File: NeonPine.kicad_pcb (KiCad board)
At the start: 2 copper layers, 54.7 x 69 mm, 74 parts, among them J1 USB-C 6P (USB4125-GF-A), J2 SWD pogo pads, Q1 DMN15H310SE, Q11 MMBTA42, Q12 MMBTA42, Q13 MMBTA42, Q14 MMBTA42, Q15 MMBTA42, Q16 MMBTA42, Q17 MMBTA42, Q18 MMBTA42, Q19 MMBTA42, Q2 TEPT4400, Q20 MMBTA42, U1 CH32V003F4P6

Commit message: incomplete big package ver
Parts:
- added C10: 100n, Capacitor_SMD:C_0603_1608Metric, B.Cu at (111.8, 84.1)
- added C9: 100n, Capacitor_SMD:C_0603_1608Metric, B.Cu at (96.1, 84.1)
- added Q21: MMBTA42, Package_TO_SOT_SMD:SOT-23, B.Cu at (101.6, 54.0)
- added Q22: MMBTA42, Package_TO_SOT_SMD:SOT-23, B.Cu at (97.1, 67.5)
- added Q23: MMBTA42, Package_TO_SOT_SMD:SOT-23, B.Cu at (106.1, 67.5)
- added Q24: MMBTA42, Package_TO_SOT_SMD:SOT-23, B.Cu at (93.6, 80.0)
- added Q25: MMBTA42, Package_TO_SOT_SMD:SOT-23, B.Cu at (101.6, 80.0)
- added Q26: MMBTA42, Package_TO_SOT_SMD:SOT-23, B.Cu at (109.6, 80.0)
- added Q27: MMBTA42, Package_TO_SOT_SMD:SOT-23, B.Cu at (87.6, 92.3)
- added Q28: MMBTA42, Package_TO_SOT_SMD:SOT-23, B.Cu at (96.6, 92.3)
- added Q29: MMBTA42, Package_TO_SOT_SMD:SOT-23, B.Cu at (106.6, 92.3)
- added Q30: MMBTA42, Package_TO_SOT_SMD:SOT-23, B.Cu at (115.6, 92.3)
- added R31: 150k, Resistor_SMD:R_0805_2012Metric, B.Cu at (98.4, 50.7)
- added R32: 150k, Resistor_SMD:R_0805_2012Metric, B.Cu at (93.9, 64.2)
- added R33: 150k, Resistor_SMD:R_0805_2012Metric, B.Cu at (102.9, 64.2)
- added R34: 150k, Resistor_SMD:R_0805_2012Metric, B.Cu at (90.4, 76.7)
- added R35: 150k, Resistor_SMD:R_0805_2012Metric, B.Cu at (98.4, 76.7)
- added R36: 150k, Resistor_SMD:R_0805_2012Metric, B.Cu at (106.4, 76.7)
- added R37: 150k, Resistor_SMD:R_0805_2012Metric, B.Cu at (84.4, 89.0)
- added R38: 150k, Resistor_SMD:R_0805_2012Metric, B.Cu at (93.4, 89.0)
- added R39: 150k, Resistor_SMD:R_0805_2012Metric, B.Cu at (103.4, 89.0)
- added R40: 150k, Resistor_SMD:R_0805_2012Metric, B.Cu at (112.4, 89.0)
- added R51: 22k, Resistor_SMD:R_0402_1005Metric, B.Cu at (101.6, 56.8)
- added R52: 22k, Resistor_SMD:R_0402_1005Metric, B.Cu at (97.1, 70.2)
- added R53: 22k, Resistor_SMD:R_0402_1005Metric, B.Cu at (106.1, 70.2)
- added R54: 22k, Resistor_SMD:R_0402_1005Metric, B.Cu at (93.6, 82.8)
- added R55: 22k, Resistor_SMD:R_0402_1005Metric, B.Cu at (101.6, 82.8)
- added R56: 22k, Resistor_SMD:R_0402_1005Metric, B.Cu at (109.6, 82.8)
- added R57: 22k, Resistor_SMD:R_0402_1005Metric, B.Cu at (87.6, 95.0)
- added R58: 22k, Resistor_SMD:R_0402_1005Metric, B.Cu at (96.6, 95.0)
- added R59: 22k, Resistor_SMD:R_0402_1005Metric, B.Cu at (106.6, 95.0)
- added R60: 22k, Resistor_SMD:R_0402_1005Metric, B.Cu at (115.6, 95.0)
- added U2: 74HC595BQ, Package_DFN_QFN:DHVQFN-16-1EP_2.5x3.5mm_P0.5mm_EP1x2mm, B.Cu at (99.8, 86.2)
- added U3: 74HC595BQ, Package_DFN_QFN:DHVQFN-16-1EP_2.5x3.5mm_P0.5mm_EP1x2mm, B.Cu at (119.4, 91.8)
- D1: value ES1D -> 200V 1A fast SOD-123F (verify P/N); footprint Diode_SMD:D_SMA -> Diode_SMD:D_SOD-123F
- D2: value SMAJ100A -> SMF100A; footprint Diode_SMD:D_SMA -> Diode_SMD:D_SOD-123F
- R41, R42, R43, R44, R45, R46, R47, R48, R49, R50: footprint Resistor_SMD:R_0603_1608Metric -> Resistor_SMD:R_0402_1005Metric
- TP3: value BUZZ/spare -> SR_CLK test
- moved D2 31.4 mm to (90.0, 107.2)
- moved TP3 30.8 mm to (90.8, 86.8), turned to -90 degrees
- moved C2 23.6 mm to (122.9, 92.9), turned to 0 degrees
- moved C1 22.4 mm to (122.9, 94.7)
- moved C4 21.2 mm to (93.0, 107.2), turned to -90 degrees
- moved J2 17.0 mm to (109.5, 91.8), turned to -90 degrees
- moved R7 14.9 mm to (104.3, 76.3)
- moved R4 14.4 mm to (108.6, 107.4)
- moved FB1 13.6 mm to (115.1, 84.1)
- moved R11 12.0 mm to (92.1, 96.1), turned to 90 degrees
- moved R3 8.93 mm to (100.0, 89.7), turned to 180 degrees
- moved R12 8.85 mm to (99.8, 96.4), turned to 0 degrees
- moved R5 7.24 mm to (103.8, 84.1), turned to 0 degrees
- moved R2 7.15 mm to (105.0, 107.4), turned to 0 degrees
- moved R9 6.65 mm to (90.3, 96.0), turned to 90 degrees
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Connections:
- net /B1 renamed Net-(Q11-B)
- net /B10 renamed Net-(Q20-B)
- net /B2 renamed Net-(Q12-B)
- net /B3 renamed Net-(Q13-B)
- net /B4 renamed Net-(Q14-B)
- net /B5 renamed Net-(Q15-B)
- net /B6 renamed Net-(Q16-B)
- net /B7 renamed Net-(Q17-B)
- net /B8 renamed Net-(Q18-B)
- net /B9 renamed Net-(Q19-B)
- net /BUZZ renamed /SR_CLK
- U1 pad 1: /LAMP10 -> /SR_LATCH
- U1 pad 12: /LAMP2 -> /LAMP5
- U1 pad 13: /LAMP5 -> /LAMP9
- U1 pad 14: /LAMP1 -> /LAMP2
- U1 pad 15: /LAMP9 -> /LAMP3
- U1 pad 16: /LAMP3 -> /LAMP6
- U1 pad 17: /LAMP6 -> /LAMP10
- U1 pad 3: unconnected-(U1-PD6-Pad3) -> /SR_DATA
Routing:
- net GND: track 208.0 -> 297.2 mm, vias 7 -> 11
- net /HV+: track 114.3 -> 176.8 mm, vias 0 -> 9
- net /SR_CLK: track 23.6 -> 68.0 mm
- net /SR_CHAIN: track 0.00 -> 31.9 mm, vias 0 -> 3
- net /LAMPA1: track 0.00 -> 30.1 mm, vias 0 -> 2
- net /VBUS_F: track 45.7 -> 16.8 mm, vias 6 -> 3
- net +5V: track 101.6 -> 129.1 mm, vias 5 -> 6
- net /LAMPA7: track 0.00 -> 24.0 mm, vias 0 -> 3
- net /LAMP1: track 58.4 -> 37.1 mm
- net /SWIO: track 31.2 -> 11.4 mm
- net /CC2: track 25.4 -> 5.78 mm
- net /LAMPA3: track 0.00 -> 19.2 mm, vias 0 -> 3
- net /CC1: track 45.8 -> 27.3 mm, vias 4 -> 3
- net /VFB: track 15.5 -> 33.8 mm, vias 2 -> 4
- net /LAMPA6: track 0.00 -> 16.7 mm, vias 0 -> 2
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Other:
- copper layers 2 -> 4

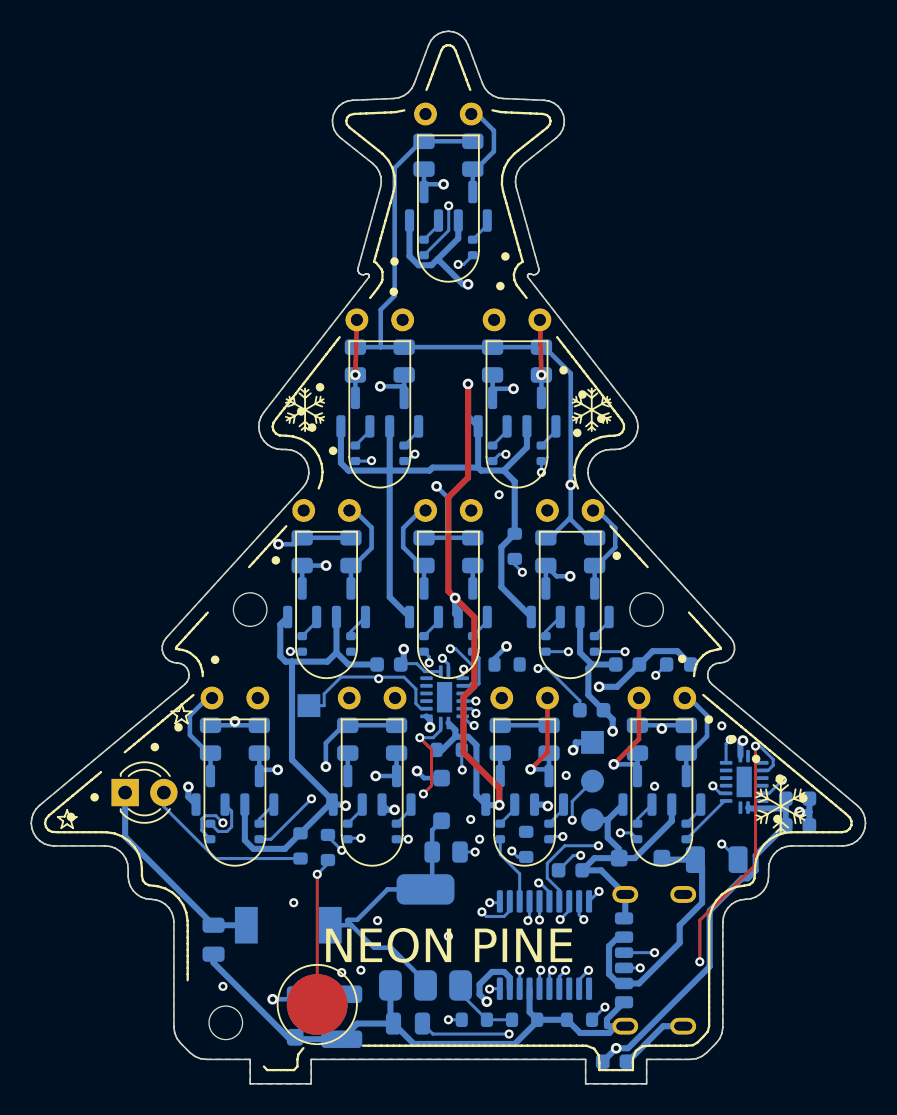
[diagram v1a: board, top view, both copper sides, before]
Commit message: 2Layer routing complete
needs cleanup
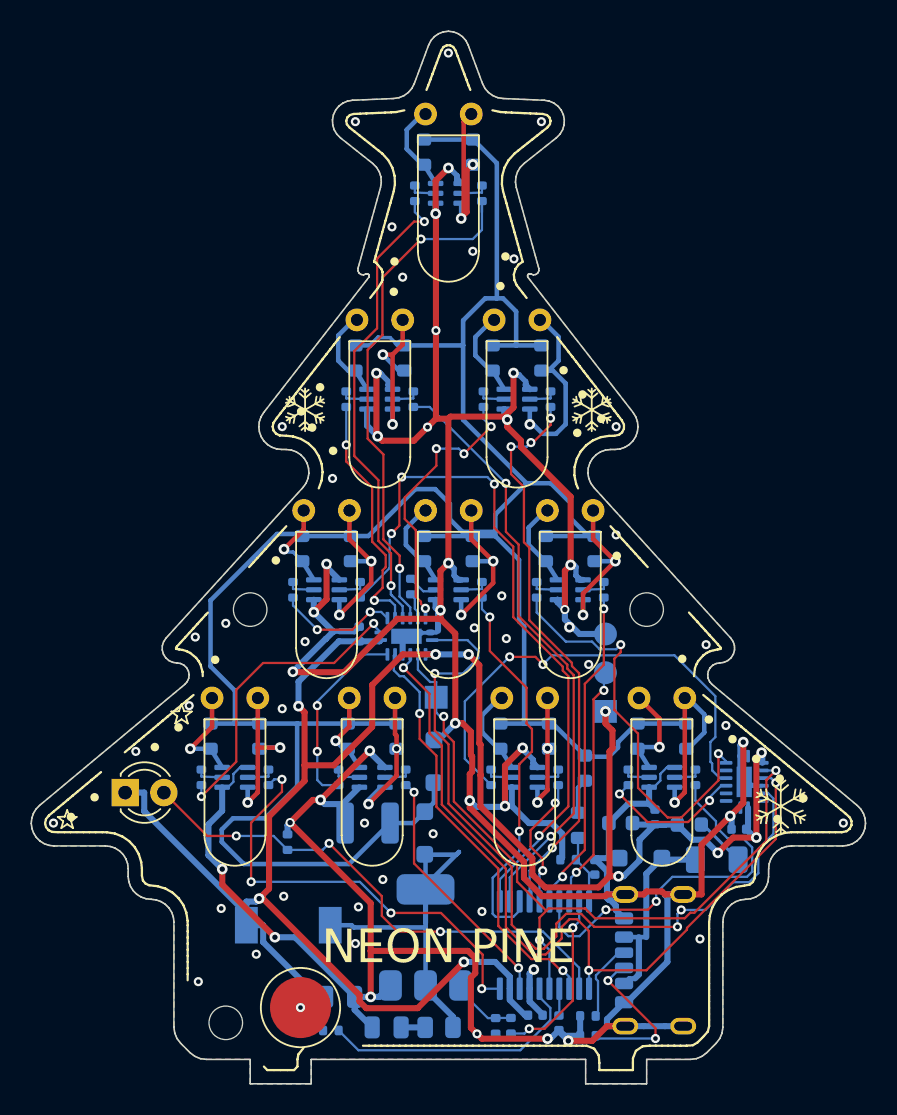
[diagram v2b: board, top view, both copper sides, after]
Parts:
- removed Q21, Q22, Q23, Q24, Q25, Q26, Q27, Q28, Q29, Q30: MMBTA42, Package_TO_SOT_SMD:SOT-23
- C10, C2, C5, C6, C7, C9: footprint Capacitor_SMD:C_0603_1608Metric -> Capacitor_SMD:C_0402_1005Metric
- Q11, Q12, Q13, Q14, Q15, Q16, Q17, Q18, Q19, Q20: value MMBTA42 -> MMDT5551; footprint Package_TO_SOT_SMD:SOT-23 -> Package_TO_SOT_SMD:SOT-363_SC-70-6
- R1, R11, R2, R3, R4, R7, R9: footprint Resistor_SMD:R_0603_1608Metric -> Resistor_SMD:R_0402_1005Metric
- R21, R22, R23, R24, R25, R26, R27, R28, R29, R30, R31, R32, R33, R34, R35, R36, R37, R38, R39, R40: value 150k -> 150k 200V; footprint Resistor_SMD:R_0805_2012Metric -> Resistor_SMD:R_0603_1608Metric
- U2, U3: footprint Package_DFN_QFN:DHVQFN-16-1EP_2.5x3.5mm_P0.5mm_EP1x2mm -> NeonPine:DHVQFN-16-1EP_2.5x3.5mm_P0.5mm_EP1x2mm_EPGND
- moved R7 20.8 mm to (107.8, 96.9), turned to 180 degrees
- moved R3 19.7 mm to (109.2, 107.2)
- moved D2 19.0 mm to (99.0, 90.5), turned to 90 degrees
- moved C10 13.0 mm to (119.0, 94.9)
- moved C4 12.8 mm to (94.7, 94.5), turned to 180 degrees
- moved R11 12.0 mm to (92.3, 108.1), turned to 0 degrees
- moved C1 11.6 mm to (111.3, 94.5), turned to 180 degrees
- moved R12 11.5 mm to (99.4, 107.9), turned to 180 degrees
- moved FB1 10.5 mm to (115.8, 94.6), turned to 180 degrees
- moved C5 10.3 mm to (109.6, 97.4), turned to 90 degrees
- moved C7 10.0 mm to (107.2, 107.6), turned to -90 degrees
- moved C2 9.43 mm to (113.5, 94.1), turned to 90 degrees
- moved C3 9.11 mm to (92.9, 105.9), turned to 0 degrees
- moved R5 8.50 mm to (109.0, 90.9), turned to -90 degrees
- moved TP3 8.37 mm to (99.2, 86.2), turned to 180 degrees
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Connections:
- LA1 pad 1: Net-(Q11-C) -> Net-(Q11A-C1)
- LA1 pad 2: Net-(Q21-C) -> Net-(Q11B-C2)
- LA10 pad 1: Net-(Q20-C) -> Net-(Q20A-C1)
- LA10 pad 2: Net-(Q30-C) -> Net-(Q20B-C2)
- LA2 pad 1: Net-(Q12-C) -> Net-(Q12A-C1)
- LA2 pad 2: Net-(Q22-C) -> Net-(Q12B-C2)
- LA3 pad 1: Net-(Q13-C) -> Net-(Q13A-C1)
- LA3 pad 2: Net-(Q23-C) -> Net-(Q13B-C2)
- LA4 pad 1: Net-(Q14-C) -> Net-(Q14A-C1)
- LA4 pad 2: Net-(Q24-C) -> Net-(Q14B-C2)
- LA5 pad 1: Net-(Q15-C) -> Net-(Q15A-C1)
- LA5 pad 2: Net-(Q25-C) -> Net-(Q15B-C2)
- LA6 pad 1: Net-(Q16-C) -> Net-(Q16A-C1)
- LA6 pad 2: Net-(Q26-C) -> Net-(Q16B-C2)
- LA7 pad 1: Net-(Q17-C) -> Net-(Q17A-C1)
- LA7 pad 2: Net-(Q27-C) -> Net-(Q17B-C2)
- LA8 pad 1: Net-(Q18-C) -> Net-(Q18A-C1)
- LA8 pad 2: Net-(Q28-C) -> Net-(Q18B-C2)
- LA9 pad 1: Net-(Q19-C) -> Net-(Q19A-C1)
- LA9 pad 2: Net-(Q29-C) -> Net-(Q19B-C2)
- Q11 pad 1: Net-(Q11-B) -> GND
- Q11 pad 2: GND -> Net-(Q11A-B1)
- Q11 pad 3: Net-(Q11-C) -> Net-(Q11B-C2)
- Q12 pad 1: Net-(Q12-B) -> GND
- Q12 pad 2: GND -> Net-(Q12A-B1)
- Q12 pad 3: Net-(Q12-C) -> Net-(Q12B-C2)
- Q13 pad 1: Net-(Q13-B) -> GND
- Q13 pad 2: GND -> Net-(Q13A-B1)
- Q13 pad 3: Net-(Q13-C) -> Net-(Q13B-C2)
- Q14 pad 1: Net-(Q14-B) -> GND
- Q14 pad 2: GND -> Net-(Q14A-B1)
- Q14 pad 3: Net-(Q14-C) -> Net-(Q14B-C2)
- Q15 pad 1: Net-(Q15-B) -> GND
- Q15 pad 2: GND -> Net-(Q15A-B1)
- Q15 pad 3: Net-(Q15-C) -> Net-(Q15B-C2)
- Q16 pad 1: Net-(Q16-B) -> GND
- Q16 pad 2: GND -> Net-(Q16A-B1)
- Q16 pad 3: Net-(Q16-C) -> Net-(Q16B-C2)
- Q17 pad 1: Net-(Q17-B) -> GND
- Q17 pad 2: GND -> Net-(Q17A-B1)
- Q17 pad 3: Net-(Q17-C) -> Net-(Q17B-C2)
- Q18 pad 1: Net-(Q18-B) -> GND
- Q18 pad 2: GND -> Net-(Q18A-B1)
- Q18 pad 3: Net-(Q18-C) -> Net-(Q18B-C2)
- Q19 pad 1: Net-(Q19-B) -> GND
- Q19 pad 2: GND -> Net-(Q19A-B1)
- Q19 pad 3: Net-(Q19-C) -> Net-(Q19B-C2)
- Q20 pad 1: Net-(Q20-B) -> GND
- Q20 pad 2: GND -> Net-(Q20A-B1)
- Q20 pad 3: Net-(Q20-C) -> Net-(Q20B-C2)
- R21 pad 2: Net-(Q21-C) -> Net-(Q11B-C2)
- R22 pad 2: Net-(Q22-C) -> Net-(Q12B-C2)
- R23 pad 2: Net-(Q23-C) -> Net-(Q13B-C2)
- R24 pad 2: Net-(Q24-C) -> Net-(Q14B-C2)
- R25 pad 2: Net-(Q25-C) -> Net-(Q15B-C2)
- R26 pad 2: Net-(Q26-C) -> Net-(Q16B-C2)
- R27 pad 2: Net-(Q27-C) -> Net-(Q17B-C2)
- R28 pad 2: Net-(Q28-C) -> Net-(Q18B-C2)
- R29 pad 2: Net-(Q29-C) -> Net-(Q19B-C2)
- R30 pad 2: Net-(Q30-C) -> Net-(Q20B-C2)
- R31 pad 2: Net-(Q11-C) -> Net-(Q11A-C1)
- R32 pad 2: Net-(Q12-C) -> Net-(Q12A-C1)
- R33 pad 2: Net-(Q13-C) -> Net-(Q13A-C1)
- R34 pad 2: Net-(Q14-C) -> Net-(Q14A-C1)
- R35 pad 2: Net-(Q15-C) -> Net-(Q15A-C1)
- R36 pad 2: Net-(Q16-C) -> Net-(Q16A-C1)
- R37 pad 2: Net-(Q17-C) -> Net-(Q17A-C1)
- R38 pad 2: Net-(Q18-C) -> Net-(Q18A-C1)
- R39 pad 2: Net-(Q19-C) -> Net-(Q19A-C1)
- R40 pad 2: Net-(Q20-C) -> Net-(Q20A-C1)
- R41 pad 2: Net-(Q11-B) -> Net-(Q11A-B1)
- R42 pad 2: Net-(Q12-B) -> Net-(Q12A-B1)
- R43 pad 2: Net-(Q13-B) -> Net-(Q13A-B1)
- R44 pad 2: Net-(Q14-B) -> Net-(Q14A-B1)
- R45 pad 2: Net-(Q15-B) -> Net-(Q15A-B1)
- R46 pad 2: Net-(Q16-B) -> Net-(Q16A-B1)
- R47 pad 2: Net-(Q17-B) -> Net-(Q17A-B1)
- R48 pad 2: Net-(Q18-B) -> Net-(Q18A-B1)
- R49 pad 2: Net-(Q19-B) -> Net-(Q19A-B1)
- R50 pad 2: Net-(Q20-B) -> Net-(Q20A-B1)
- R51 pad 2: Net-(Q21-B) -> Net-(Q11B-B2)
- R52 pad 2: Net-(Q22-B) -> Net-(Q12B-B2)
- R53 pad 2: Net-(Q23-B) -> Net-(Q13B-B2)
- R54 pad 2: Net-(Q24-B) -> Net-(Q14B-B2)
- R55 pad 2: Net-(Q25-B) -> Net-(Q15B-B2)
- R56 pad 2: Net-(Q26-B) -> Net-(Q16B-B2)
- R57 pad 2: Net-(Q27-B) -> Net-(Q17B-B2)
- R58 pad 2: Net-(Q28-B) -> Net-(Q18B-B2)
- R59 pad 2: Net-(Q29-B) -> Net-(Q19B-B2)
- R60 pad 2: Net-(Q30-B) -> Net-(Q20B-B2)
- U1 pad 12: /LAMP5 -> /LAMP2
- U1 pad 13: /LAMP9 -> /LAMP5
- U1 pad 14: /LAMP2 -> /LAMP3
- U1 pad 15: /LAMP3 -> /LAMP9
- U2 pad 1: /LAMPA2 -> /LAMPA7
- U2 pad 15: /LAMPA4 -> /LAMPA8
- U2 pad 2: /LAMPA1 -> /LAMPA4
- U2 pad 3: /LAMP1 -> /LAMPA2
- U2 pad 4: /LAMPA5 -> /LAMPA1
- U2 pad 5: /LAMPA3 -> /LAMP1
- U2 pad 6: /LAMPA7 -> /LAMPA5
- U2 pad 7: /LAMPA8 -> /LAMPA3
- U3 pad 2: /LAMPA10 -> unconnected-(U3-QC-Pad2)
- U3 pad 3: /LAMPA9 -> unconnected-(U3-QD-Pad3)
- U3 pad 4: unconnected-(U3-QE-Pad4) -> /LAMPA10
- U3 pad 5: unconnected-(U3-QF-Pad5) -> /LAMPA9
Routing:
- net /SR_LATCH: track 0.00 -> 53.2 mm, vias 0 -> 3
- net /VFB: track 33.8 -> 4.95 mm, vias 4 -> 0
- net /SR_DATA: track 0.00 -> 27.7 mm, vias 0 -> 2
- net /CC1: track 27.3 -> 5.24 mm, vias 3 -> 0
- net /SR_CHAIN: track 31.9 -> 52.4 mm
- net /SR_CLK: track 68.0 -> 48.9 mm, vias 4 -> 3
- net Net-(C8-Pad1): track 19.8 -> 1.57 mm, vias 2 -> 0
- net /LAMP4: track 30.9 -> 46.5 mm, vias 3 -> 4
- net /LAMPA9: track 16.1 -> 31.6 mm, vias 3 -> 2
- net /LAMP10: track 9.74 -> 24.5 mm
- net /HV+: track 176.8 -> 163.0 mm, vias 9 -> 0
- net /LDR: track 48.1 -> 34.5 mm, vias 1 -> 3
- net /VBUS_F: track 16.8 -> 3.37 mm, vias 3 -> 0
- net Net-(Q13B-C2): track 0.00 -> 13.1 mm, vias 0 -> 1
- net Net-(Q20B-C2): track 0.00 -> 12.7 mm, vias 0 -> 1
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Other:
- copper layers 4 -> 2

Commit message: finished routing, check and sim
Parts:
- added R13: 33, Resistor_SMD:R_0402_1005Metric, B.Cu at (106.5, 98.0)
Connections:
- U1 pad 15: /LAMP9 -> /SR_SCK
- U1 pad 16: /LAMP6 -> /SR_DATA
- U1 pad 3: /SR_DATA -> /LAMP6
- U1 pad 5: /SR_CLK -> /LAMP9
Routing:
- net /LAMP6: track 21.4 -> 39.8 mm, vias 2 -> 4
- net /LAMP9: track 8.79 -> 20.5 mm, vias 2 -> 4
- net /SW: track 26.6 -> 21.2 mm
- net /SR_CLK: track 48.9 -> 44.5 mm
- net /SR_LATCH: track 53.2 -> 49.1 mm
- net /SR_CHAIN: track 52.4 -> 48.4 mm, vias 3 -> 2
- net /SR_SCK: track 0.00 -> 2.04 mm
- net /LAMPA6: track 27.5 -> 26.1 mm
- net /LAMP1: track 34.3 -> 33.6 mm
- net GND: track 290.4 -> 290.1 mm, vias 68 -> 73
- net Net-(Q13B-C2): vias 1 -> 0
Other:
- board text added: "G"

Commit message: cheaper components
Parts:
- C1: value 10u -> 10uF
- C10, C2, C6, C7, C9: value 100n -> 100nF
- C3: value 22u 10V -> 22uF 10V
- C4: value 1u 250V -> 1uF 250V
- C5: value 10n -> 10nF
- C8: value 100p C0G 250V -> 100pF 250V C0G
- D1: value 200V 1A fast SOD-123F (verify P/N) -> 200V 1A fast recovery
- D3: value SMF5.0A (TVS) -> SMF5.0A
- F1: value PTC 0.5A (MF-NSMF050-2) -> MF-NSMF050-2
- FB1: value 600R@100MHz -> 600Ω@100MHz
- J1: value USB-C 6P (USB4125-GF-A) -> USB4125-GF-A
- L11: value 330u (SWPA6028S331MT, Isat>=0.4A) -> 330uH
- R1: value 47 -> 47Ω
- R11: value 1k -> 1kΩ
- R12: value 100 (snubber) -> 100Ω
- R13: value 33 -> 33Ω
- R2: value 100k -> 100kΩ
- R21, R22, R23, R24, R25, R26, R27, R28, R29, R30, R31, R32, R33, R34, R35, R36, R37, R38, R39, R40: value 150k 200V -> 150kΩ 200V
- R3, R4: value 5k1 -> 5.1kΩ
- R41, R42, R43, R44, R45, R46, R47, R48, R49, R50, R51, R52, R53, R54, R55, R56, R57, R58, R59, R60, R9: value 22k -> 22kΩ
- R5, R6: value 1M -> 1MΩ
- R7: value 39k -> 39kΩ
